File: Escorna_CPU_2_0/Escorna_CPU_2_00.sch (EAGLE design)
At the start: 58 parts, among them IC1 ULN2803, U2 ESP01, X1 AK550/2

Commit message: Act. bottom layer
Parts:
- Z1: value F/CM12P -> CFG12
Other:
- note added: "006"
- note removed: "005"
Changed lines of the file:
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@@
 <part name="FRAME1" library="frames" deviceset="DINA4_L" device=""/>
 <part name="IC1" library="uln-udn" deviceset="ULN2803A" device="&quot;" value="ULN2803"/>
-<part name="Z1" library="buzzer" deviceset="F/CM12P" device=""/>
+<part name="Z1" library="buzzer" deviceset="F/CM12P" device="" value="CFG12"/>
 <part name="SUPPLY2" library="supply2" deviceset="GND" device=""/>
 <part name="SUPPLY3" library="supply2" deviceset="GND" device=""/>
@@
 Sx.1 = 12mm
 </text>
-<text x="254" y="7.62" size="2.54" layer="97">005</text>
+<text x="254" y="7.62" size="2.54" layer="97">006</text>
 </plain>
 <instances>

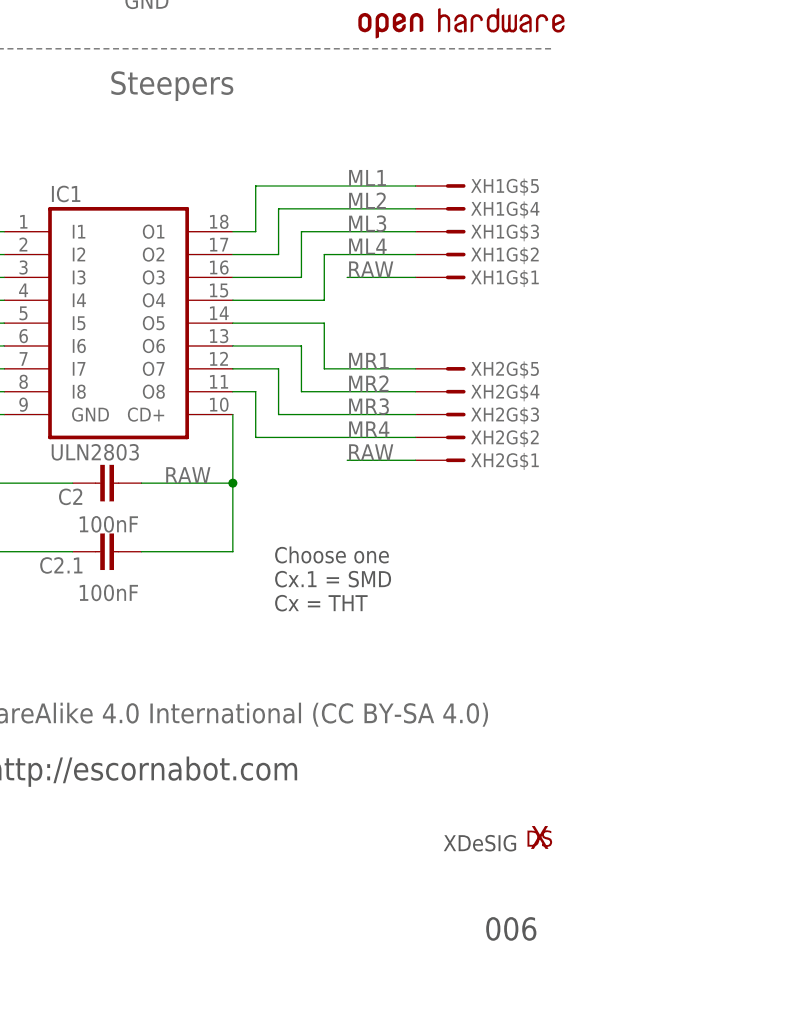
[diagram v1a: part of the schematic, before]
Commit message: Act. slikscreen
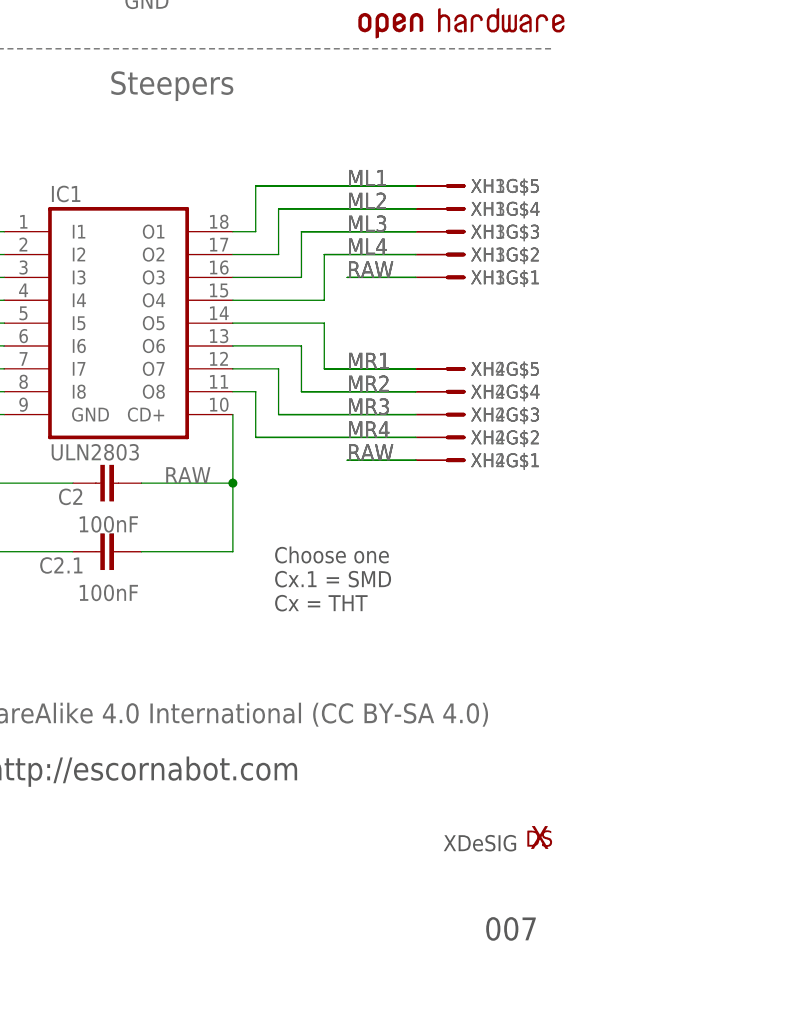
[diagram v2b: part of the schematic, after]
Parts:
- added XH3, XH4: (no value), con-jst:B5B-XH-A
- S6: device escorna:SK12F14F -> escorna:SK12F14D
- renumbered XDS to XDS1
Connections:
- net ML1: now also XH3G$5.1
- net ML2: now also XH3G$4.1
- net ML3: now also XH3G$3.1
- net ML4: now also XH3G$2.1
- net MR1: now also XH4G$5.1
- net MR2: now also XH4G$4.1
- net MR3: now also XH4G$3.1
- net MR4: now also XH4G$2.1
- net RAW: now also XH3G$1.1, XH4G$1.1
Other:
- note added: "007"
- note removed: "006"
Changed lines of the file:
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@@
 <part name="H2" library="holes" deviceset="MOUNT-HOLE" device="3.0"/>
 <part name="LOGO1" library="SparkFun-Aesthetics" deviceset="OSHW-LOGO" device="S"/>
-<part name="XDS" library="xdesig" deviceset="XDESIG" device=""/>
+<part name="XDS1" library="xdesig" deviceset="XDESIG" device=""/>
 <part name="ESC" library="escorna" deviceset="ESCORNABOT" device=""/>
-<part name="S6" library="escorna" deviceset="SK12F14" device="F"/>
+<part name="S6" library="escorna" deviceset="SK12F14" device="D"/>
 <part name="R1" library="rcl" deviceset="R-EU_" device="0204/7" value="10K"/>
 <part name="R2" library="rcl" deviceset="R-EU_" device="0204/7" value="10K"/>
@@
 <part name="RN4" library="resistor-dil" deviceset="4R-N" device="CAY16" value="1K"/>
 <part name="SUPPLY8" library="supply2" deviceset="GND" device=""/>
+<part name="XH3" library="con-jst" deviceset="B5B-XH-A" device=""/>
+<part name="XH4" library="con-jst" deviceset="B5B-XH-A" device=""/>
 </parts>
 <sheets>
@@
 Sx.1 = 12mm
 </text>
-<text x="254" y="7.62" size="2.54" layer="97">006</text>
+<text x="254" y="7.62" size="2.54" layer="97">007</text>
 </plain>
 <instances>
@@
 <instance part="H2" gate="G$1" x="137.16" y="27.94"/>
 <instance part="LOGO1" gate="G$1" x="251.46" y="116.84"/>
-<instance part="XDS" gate="G$1" x="259.08" y="17.78"/>
+<instance part="XDS1" gate="G$1" x="259.08" y="17.78"/>
 <instance part="ESC" gate="G$1" x="119.38" y="7.62"/>
 <instance part="S6" gate="S$" x="44.196" y="22.86" rot="MR0"/>
@@
 <instance part="RN4" gate="D" x="200.66" y="134.62" rot="R270"/>
 <instance part="SUPPLY8" gate="GND" x="215.9" y="114.3"/>
+<instance part="XH3" gate="G$1" x="251.46" y="81.28"/>
+<instance part="XH3" gate="G$2" x="251.46" y="83.82"/>
+<instance part="XH3" gate="G$3" x="251.46" y="86.36"/>
+<instance part="XH3" gate="G$4" x="251.46" y="88.9"/>
+<instance part="XH3" gate="G$5" x="251.46" y="91.44"/>
+<instance part="XH4" gate="G$1" x="251.46" y="60.96"/>
+<instance part="XH4" gate="G$2" x="251.46" y="63.5"/>
+<instance part="XH4" gate="G$3" x="251.46" y="66.04"/>
+<instance part="XH4" gate="G$4" x="251.46" y="68.58"/>
+<instance part="XH4" gate="G$5" x="251.46" y="71.12"/>
 </instances>
 <busses>
@@
 <pinref part="XH2" gate="G$5" pin="1"/>
 </segment>
+<segment>
+<wire x1="246.38" y1="71.12" x2="236.22" y2="71.12" width="0.1524" layer="91"/>
+<label x="238.76" y="71.12" size="1.778" layer="95"/>
+<pinref part="XH4" gate="G$5" pin="1"/>
+</segment>
 </net>
 <net name="MR2" class="0">
@@
 <pinref part="XH2" gate="G$4" pin="1"/>
 </segment>
+<segment>
+<wire x1="246.38" y1="68.58" x2="233.68" y2="68.58" width="0.1524" layer="91"/>
+<label x="238.76" y="68.58" size="1.778" layer="95"/>
+<pinref part="XH4" gate="G$4" pin="1"/>
+</segment>
 </net>
 <net name="MR3" class="0">
@@
 <pinref part="XH2" gate="G$3" pin="1"/>
 </segment>
+<segment>
+<label x="238.76" y="66.04" size="1.778" layer="95"/>
+<wire x1="246.38" y1="66.04" x2="231.14" y2="66.04" width="0.1524" layer="91"/>
+<pinref part="XH4" gate="G$3" pin="1"/>
+</segment>
 </net>
 <net name="MR4" class="0">
@@
 <pinref part="XH2" gate="G$2" pin="1"/>
 </segment>
+<segment>
+<label x="238.76" y="63.5" size="1.778" layer="95"/>
+<wire x1="228.6" y1="63.5" x2="246.38" y2="63.5" width="0.1524" layer="91"/>
+<pinref part="XH4" gate="G$2" pin="1"/>
+</segment>
 </net>
 <net name="D10" class="0">
@@
 <pinref part="XH1" gate="G$2" pin="1"/>
 </segment>
+<segment>
+<wire x1="246.38" y1="83.82" x2="236.22" y2="83.82" width="0.1524" layer="91"/>
+<label x="238.76" y="83.82" size="1.778" layer="95"/>
+<pinref part="XH3" gate="G$2" pin="1"/>
+</segment>
 </net>
 <net name="ML3" class="0">
@@
 <pinref part="XH1" gate="G$3" pin="1"/>
 </segment>
+<segment>
+<wire x1="246.38" y1="86.36" x2="233.68" y2="86.36" width="0.1524" layer="91"/>
+<label x="238.76" y="86.36" size="1.778" layer="95"/>
+<pinref part="XH3" gate="G$3" pin="1"/>
+</segment>
 </net>
 <net name="ML2" class="0">
@@
 <pinref part="XH1" gate="G$4" pin="1"/>
 </segment>
+<segment>
+<wire x1="246.38" y1="88.9" x2="231.14" y2="88.9" width="0.1524" layer="91"/>
+<label x="238.76" y="88.9" size="1.778" layer="95"/>
+<pinref part="XH3" gate="G$4" pin="1"/>
+</segment>
 </net>
 <net name="ML1" class="0">
@@
 <wire x1="228.6" y1="86.36" x2="226.06" y2="86.36" width="0.1524" layer="91"/>
 <pinref part="XH1" gate="G$5" pin="1"/>
+</segment>
+<segment>
+<label x="238.76" y="91.44" size="1.778" layer="95"/>
+<wire x1="246.38" y1="91.44" x2="228.6" y2="91.44" width="0.1524" layer="91"/>
+<pinref part="XH3" gate="G$5" pin="1"/>
 </segment>
 </net>
@@
 <label x="43.18" y="86.36" size="1.778" layer="95"/>
 </segment>
-</net>
+<segment>
+<wire x1="246.38" y1="81.28" x2="238.76" y2="81.28" width="0.1524" layer="91"/>
+<label x="238.76" y="81.28" size="1.778" layer="95"/>
+<pinref part="XH3" gate="G$1" pin="1"/>
+</segment>
+<segment>
+<wire x1="246.38" y1="60.96" x2="238.76" y2="60.96" width="0.1524" layer="91"/>
+<label x="238.76" y="60.96" size="1.778" layer="95"/>
+<pinref part="XH4" gate="G$1" pin="1"/>
+</segment>
+</net>
